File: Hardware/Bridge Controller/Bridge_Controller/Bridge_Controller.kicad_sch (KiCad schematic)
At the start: 50 parts, among them J1 AVR-UPDI-6, J2 Conn_02x08_standard_header_fo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, J3 Conn_02x08_standard_header_fo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, J4 USB_C_Receptacle_USB2.0_16P, SW1 SW_Push, U1 AVR128DA64x-xPT, U2 FT231XQ

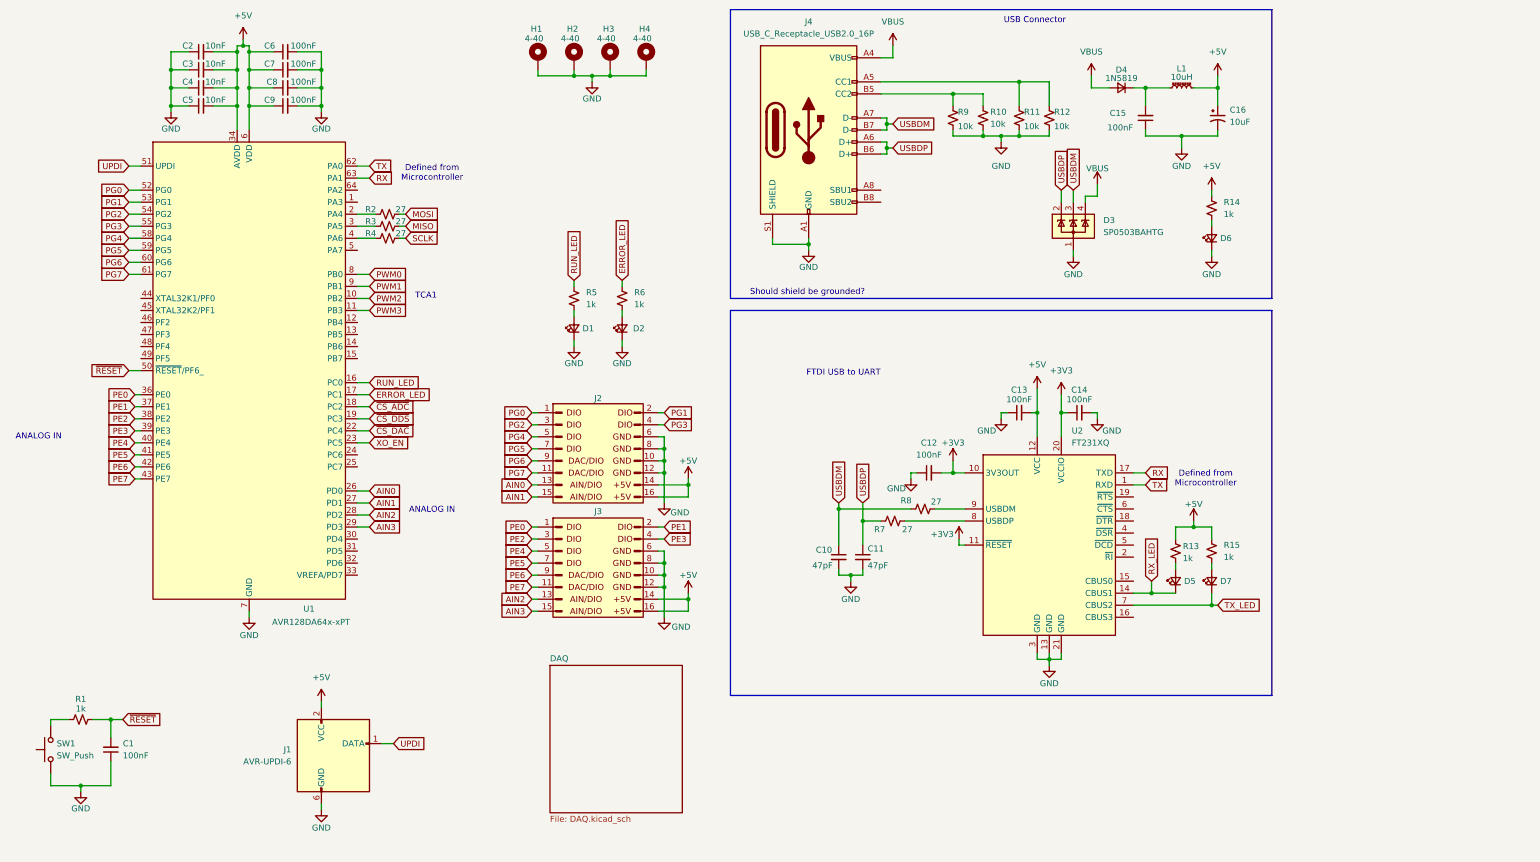
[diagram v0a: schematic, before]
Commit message: Need to update TX/RX level for UART communication
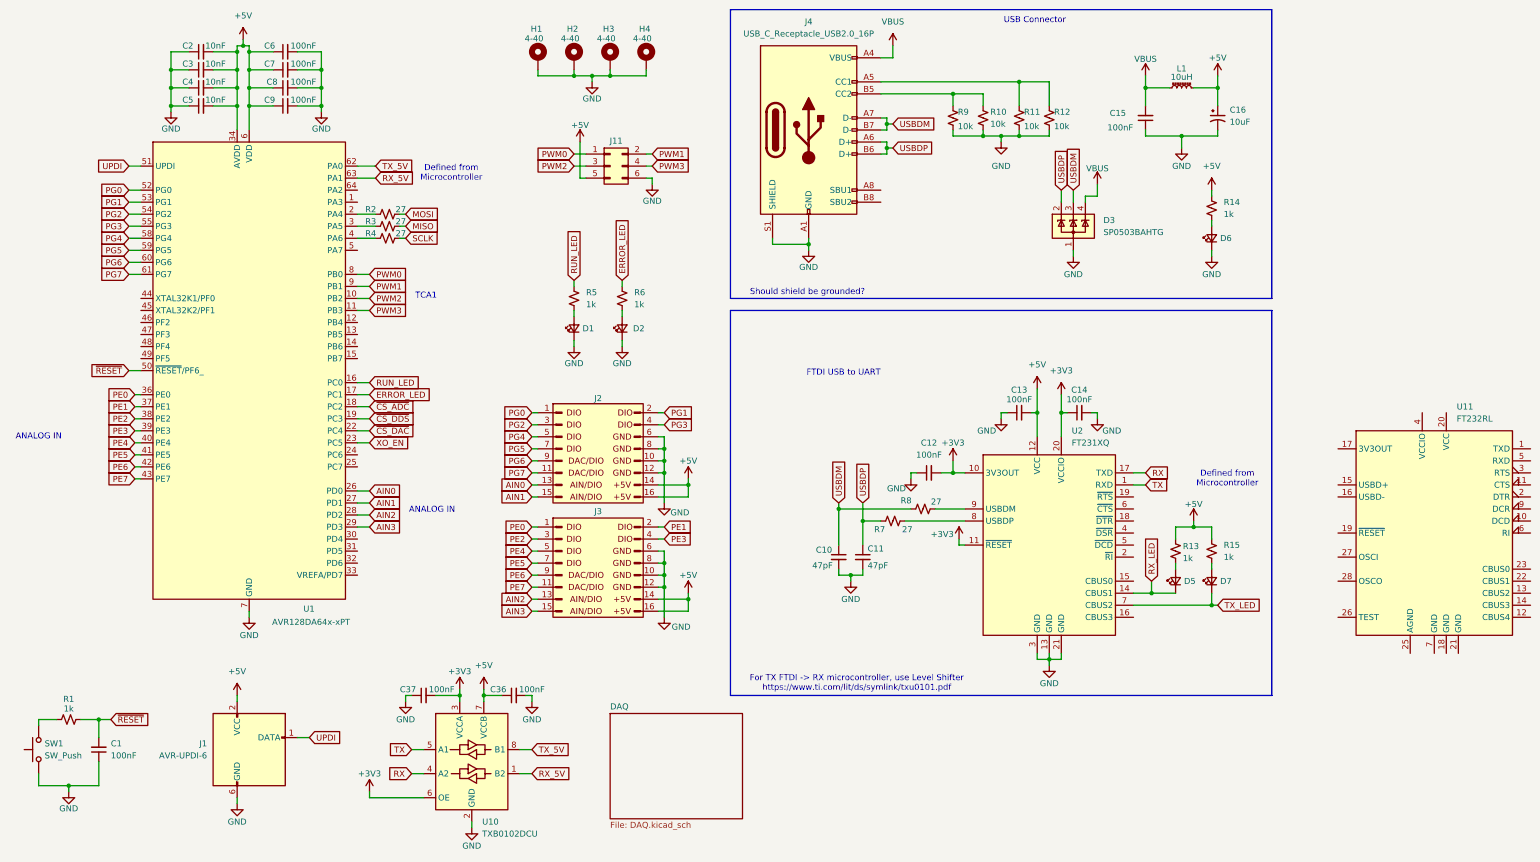
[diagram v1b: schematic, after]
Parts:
- removed D4: 1N5819, Diode_SMD:D_SOD-123, symbol Device:D_Small
- added C36, C37: 100nF, Capacitor_SMD:C_0603_1608Metric, symbol Device:C_Small
- added J11: PWM, symbol Connector_Generic:Conn_02x03_Odd_Even
- added U10: TXB0102DCU, Package_SO:VSSOP-8_2.4x2.1mm_P0.5mm, symbol Logic_LevelTranslator:TXB0102DCU
- added U11: FT232RL, Package_SO:SSOP-28_5.3x10.2mm_P0.65mm, symbol Interface_USB:FT232RL
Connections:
- net +3V3: now also C37.2, U10.3 (VCCA), U10.6 (OE)
- net +5V: now also C36.1, J11.5 (Pin_5), U10.7 (VCCB)
- net GND: now also C36.2, C37.1, J11.6 (Pin_6), U10.2 (GND)
- net PWM0: now also J11.1 (Pin_1)
- net PWM1: now also J11.2 (Pin_2)
- net PWM2: now also J11.3 (Pin_3)
- net PWM3: now also J11.4 (Pin_4)
- net RX: now also U10.4 (A2); no longer U1.63 (PA1)
- net TX: now also U10.5 (A1); no longer U1.62 (PA0)
- net VBUS: now also C15.2, L1.1
- new net RX_5V: U1.63 (PA1), U10.1 (B2)
- new net TX_5V: U1.62 (PA0), U10.8 (B1)
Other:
- note added: "For TX FTDI -> RX microcontroller, use Level Shifter https://www.ti.com/lit/ds/symlink/txu0101.pdf"
- moved on the sheet: C1, J1, R1, SW1

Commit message: Updating FTDI controller for +5V RX and TX
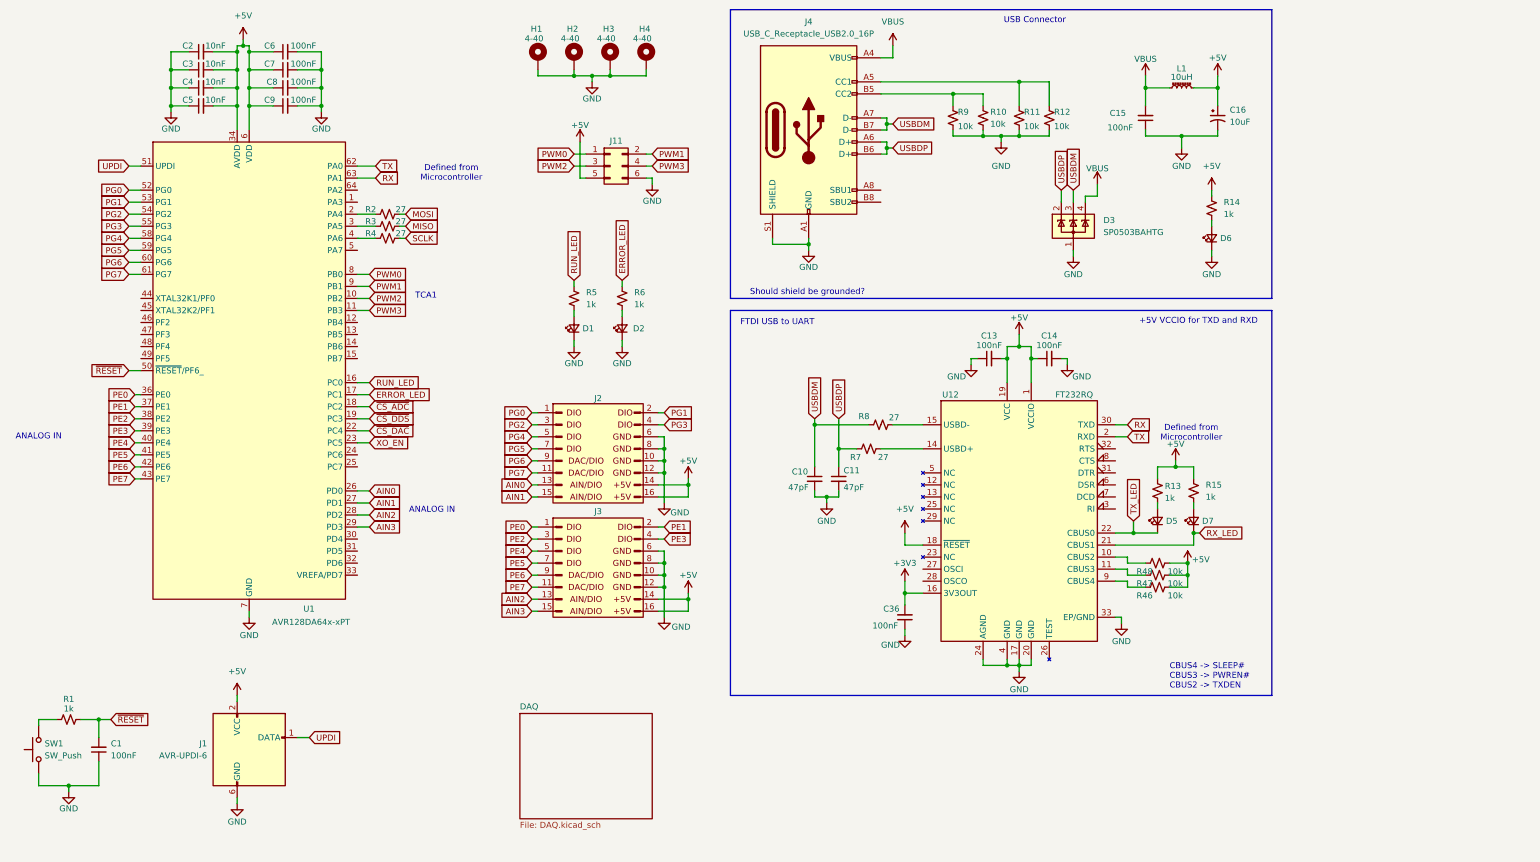
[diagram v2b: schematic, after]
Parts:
- removed C12, C37: 100nF, Capacitor_SMD:C_0603_1608Metric, symbol Device:C_Small
- removed U10: TXB0102DCU, Package_SO:VSSOP-8_2.4x2.1mm_P0.5mm, symbol Logic_LevelTranslator:TXB0102DCU
- removed U11: FT232RL, Package_SO:SSOP-28_5.3x10.2mm_P0.65mm, symbol Interface_USB:FT232RL
- removed U2: FT231XQ, Package_DFN_QFN:QFN-20-1EP_4x4mm_P0.5mm_EP2.5x2.5mm, symbol Interface_USB:FT231XQ
- added R46, R47, R48: 10k, Resistor_SMD:R_0603_1608Metric, symbol Device:R_Small_US
- added U12: FT232RQ, Package_DFN_QFN:QFN-32-1EP_5x5mm_P0.5mm_EP3.1x3.1mm, symbol _tim-Interface:FT232RQ
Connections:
- net RX_5V is gone; now on net RX: U1.63 (PA1)
- net TX_5V is gone; now on net TX: U1.62 (PA0)
- net +3V3: now also C36.2, U12.16 (3V3OUT); no longer C14.1
- net +5V: now also C14.1, R46.2, R47.2, R48.2, U12.1 (VCCIO), U12.18 (~{RESET}), U12.19 (VCC); no longer C36.1
- net GND: now also C36.1, U12.17 (GND), U12.20 (GND), U12.24 (AGND), U12.33 (EP/GND), U12.4 (GND); no longer C36.2
- net RX: now also U12.30 (TXD)
- net RX_LED: now also D7.1 (K), U12.21 (CBUS1); no longer D5.1 (K)
- net TX: now also U12.2 (RXD)
- net TX_LED: now also D5.1 (K), U12.22 (CBUS0); no longer D7.1 (K)
- net at R7.2: now also U12.14 (USBD+)
- net at R8.2: now also U12.15 (USBD-)
- new net: R46.1, U12.9 (CBUS4)
- new net: R48.1, U12.10 (CBUS2)
- new net: R47.1, U12.11 (CBUS3)
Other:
- note added: "+5V VCCIO for TXD and RXD"
- note added: "CBUS4 -> SLEEP# CBUS3 -> PWREN# CBUS2 -> TXDEN"
- note removed: "For TX FTDI -> RX microcontroller, use Level Shifter https://www.ti.com/lit/ds/symlink/txu0101.pdf"
- moved on the sheet: C10, C11, C13, C14, D5, D7, R13, R15, R7, R8

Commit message: Finalizing Board Routing
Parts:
- J4: renamed from J11; footprint (none) -> Connector_PinHeader_2.54mm:PinHeader_2x03_P2.54mm_Vertical
- renumbered C36 to C12, D5 to D4, D7 to D5, J4 to J5, R48 to R14, R47 to R15, R46 to R16, R15 to R17, R14 to R18, U12 to U2
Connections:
- net PWM0 renamed PB0
- net PWM1 renamed PB1
- net PWM2 renamed PB2
- net PWM3 renamed PB3
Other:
- note added: "For PWM"

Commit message: Updating BOM
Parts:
- added TP8: TestPoint, TestPoint:TestPoint_Pad_D1.0mm, symbol Connector:TestPoint
- C1, C12, C13, C14, C15, C6, C7, C8, C9: Digikey (none) -> 490-4779-1-ND
- C10, C11: Digikey (none) -> 490-4944-1-ND
- C16: Digikey (none) -> 399-3684-1-ND
- C2, C3, C4, C5: Digikey (none) -> 490-4778-1-ND
- D1, D4, D5, D6: Digikey (none) -> 732-4986-1-ND
- D2: Digikey (none) -> 732-4985-1-ND
- J1, J4: Digikey (none) -> 609-3234-ND
- R1, R13, R17, R18, R5, R6: Digikey (none) -> 311-1.00KHRCT-ND
- R10, R11, R12, R14, R15, R16, R9: Digikey (none) -> 311-10.0KHRCT-ND
- R2, R3, R4, R7, R8: Digikey (none) -> 311-27GRCT-ND
- SW1: Digikey (none) -> SW1203CT-ND
- U1: Digikey (none) -> 150-AVR128DA64T-I/PTCT-ND
- U2: Digikey (none) -> 768-1307-ND
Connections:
- net +5V: now also TP8.1

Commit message: Minor Updates to Board
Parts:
- R14, R15, R16: now not fitted
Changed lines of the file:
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@@
 		(in_bom yes)
 		(on_board yes)
-		(dnp no)
+		(dnp yes)
 		(property "Reference" "R16"
 			(at 255.524 140.208 90)
@@
 		(in_bom yes)
 		(on_board yes)
-		(dnp no)
+		(dnp yes)
 		(property "Reference" "R14"
 			(at 255.524 135.128 90)
@@
 		(in_bom yes)
 		(on_board yes)
-		(dnp no)
+		(dnp yes)
 		(property "Reference" "R15"
 			(at 255.524 137.668 90)

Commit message: Adding gerbers
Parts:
- J2, J3: Digikey (none) -> 900-0702461602-ND
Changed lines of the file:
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@@
 			)
 		)
+		(property "Digikey" "900-0702461602-ND"
+			(at 130.81 109.22 0)
+			(effects
+				(font
+					(size 1.27 1.27)
+				)
+				(hide yes)
+			)
+		)
 		(pin "9"
 		)
@@
 			(at 130.81 133.35 0)
 			(effects
+				(font
+					(size 1.27 1.27)
+				)
+				(hide yes)
+			)
+		)
+		(property "Digikey" "900-0702461602-ND"
+			(at 130.81 133.35 0)
+			(effects
